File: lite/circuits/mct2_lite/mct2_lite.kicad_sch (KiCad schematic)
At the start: 1 part

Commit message: 20250410-1
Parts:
- added BT?: Battery_Cell, symbol Device:Battery_Cell
- added J?: External BIOS, symbol Connector_Generic:Conn_02x04_Counter_Clockwise
- added J?: TPM, symbol Connector_Generic:Conn_02x05_Odd_Even
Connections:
- net GND: now also BT?.2 (-), J?.4 (Pin_4)
- net SOM_PWRBTN: now reaches A?.1 (~{PWRBTN})
- net SOM_SIO_UART_TX: now reaches A?.10 (SIO_UART_TX)
- net SOM_SMB_ALT: now reaches A?.104 (~{SMB_ALERT})
- net SOM_SMB_SCL: now reaches A?.106 (SMB_CLK)
- net SOM_SMB_SDA: now reaches A?.108 (SMB_DATA)
- net SOM_RTC_BAT: now reaches A?.115 (VBAT)
- net SOM_RTC_BAT: now also BT?.1 (+)
- net SOM_SIO_UART_RX: now reaches A?.12 (SIO_UART_RX)
- net SOM_UART0_RX: now reaches A?.137 (UART0_RXD)
- net SOM_UART2_TX: now reaches A?.138 (UART2_TXD)
- net SOM_UART0_TX: now reaches A?.139 (UART0_TXD)
- net SOM_UART2_RX: now reaches A?.140 (UART2_RXD)
- net SOM_UART1_RX: now reaches A?.141 (UART1_RXD)
- net SOM_UART1_TX: now reaches A?.143 (UART1_TXD)
- net SOM_SML_SDA: now reaches A?.145 (SML1_DATA)
- net SOM_SML_SCL: now reaches A?.147 (SML1_CLK)
- net SOM_SML_ALT: now reaches A?.149 (~{SML1_ALERT})
- net SOM_I2C2_SCL: now reaches A?.154 (I2C2_SCL)
- net SOM_I2C2_SDA: now reaches A?.156 (I2C2_SDA)
- net HDMI_SDA: now reaches A?.169 (DDIB_DDC_SDA)
- net HDMI_SCL: now reaches A?.171 (DDIB_DDC_SCL)
- net HDMI_HPD: now reaches A?.183 (DDIB_HPD)
- net HDMI_AUX_N: now reaches A?.191 (DDIB_AUX-)
- net HDMI_AUX_P: now reaches A?.193 (DDIB_AUX+)
- net HDMI_CLK_N: now reaches A?.197 (DDIB_TX3-)
- net HDMI_CLK_P: now reaches A?.199 (DDIB_TX3+)
- net SOM_FAN1_PWM: now reaches A?.2 (FAN1_PWM)
- net HDMI_TX2_N: now reaches A?.203 (DDIB_TX2-)
- net HDMI_TX2_P: now reaches A?.205 (DDIB_TX2+)
- net HDMI_TX1_N: now reaches A?.209 (DDIB_TX1-)
- net HDMI_TX1_P: now reaches A?.211 (DDIB_TX1+)
- net HDMI_TX0_N: now reaches A?.215 (DDIB_TX0-)
- net HDMI_TX0_P: now reaches A?.217 (DDIB_TX0+)
- net TCP1_TX0_P: now reaches A?.220 (TCP1_TX0+)
- net TCP0_AUX_N: now reaches A?.221 (TCP0_AUX-)
- net TCP1_TX0_N: now reaches A?.222 (TCP1_TX0-)
- net TCP0_AUX_P: now reaches A?.223 (TCP0_AUX+)
- net TCP1_TXRX0_P: now reaches A?.226 (TCP1_TXRX0+)
- net TCP0_TXRX1_N: now reaches A?.227 (TCP0_TXRX1-)
- net TCP1_TXRX0_N: now reaches A?.228 (TCP1_TXRX0-)
- net TCP0_TXRX1_P: now reaches A?.229 (TCP0_TXRX1+)
- net TCP1_TX1_P: now reaches A?.232 (TCP1_TX1+)
- net TCP0_TX1_N: now reaches A?.233 (TCP0_TX1-)
- net TCP1_TX1_N: now reaches A?.234 (TCP1_TX1-)
- net TCP0_TX1_P: now reaches A?.235 (TCP0_TX1+)
- net TCP1_TXRX1_P: now reaches A?.238 (TCP1_TXRX1+)
- net TCP0_TXRX0_N: now reaches A?.239 (TCP0_TXRX0-)
- net TCP1_TXRX1_N: now reaches A?.240 (TCP1_TXRX1-)
- net TCP0_TXRX0_P: now reaches A?.241 (TCP0_TXRX0+)
- net TCP1_AUX_P: now reaches A?.244 (TCP1_AUX+)
- net TCP0_TX0_N: now reaches A?.245 (TCP0_TX0-)
- net TCP1_AUX_N: now reaches A?.246 (TCP1_AUX-)
- net TCP0_TX0_P: now reaches A?.247 (TCP0_TX0+)
- net SOM_RSTBTN: now reaches A?.3 (~{RSTBTN})
- net SOM_FAN1_TAC: now reaches A?.4 (FAN1_TAC)
- net SOM_SIO_SLS_S0: now reaches A?.5 (SLS_S0)
- net SOM_FAN2_PWM: now reaches A?.6 (FAN2_PWM)
- net SOM_SIO_SLS_S3: now reaches A?.7 (SLS_S3)
- net SOM_FAN2_TAC: now reaches A?.8 (FAN2_TAC)
- net SOM_PCIE_REF0_P: now reaches A?.85 (REFCLK0+)
- net SOM_PCIE_REF0_N: now reaches A?.87 (REFCLK0-)
- net SOM_PCIE_REF3_P: now reaches A?.88 (REFCLK3+)
- net SOM_TSENSE: now reaches A?.9 (TSENSE)
- net SOM_PCIE_REF3_N: now reaches A?.90 (REFCLK3-)
- net SOM_PCIE_REF1_P: now reaches A?.91 (REFCLK1+)
- net SOM_PCIE_REF1_N: now reaches A?.93 (REFCLK1-)
- net SOM_PCIE_REF4_P: now reaches A?.94 (REFCLK4+)
- net SOM_PCIE_REF4_N: now reaches A?.96 (REFCLK4-)
- net SOM_PCIE_REF2_P: now reaches A?.97 (REFCLK2+)
- net SOM_PCIE_REF2_N: now reaches A?.99 (REFCLK2-)
- new net SOM_SPI_CLK: J?.6 (Pin_6)
- new net SOM_SPI_CS: J?.1 (Pin_1)
- new net SOM_SPI_IO0_MOSI: J?.5 (Pin_5)
- new net SOM_SPI_IO1_MISO: J?.2 (Pin_2)
- new net SOM_SPI_IO2: J?.3 (Pin_3)
- new net SOM_SPI_IO3: J?.7 (Pin_7)
- new net SOM_SPI_VCC: J?.1 (Pin_1), J?.8 (Pin_8)
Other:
- note added: "2025-03-23 - 2025-03-29"
- note added: "MediaCow Touch 2 Lite - Root"
- note removed: "2025-03-23 - 2025-03-23"
- note removed: "MediaCow Touch 2 - Root"

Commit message: 20250410-2
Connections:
- net SOM_USB2_P1_P: now also A?.69 (USB2_P1+)
- net SOM_USB_OC: now also A?.129 (~{USB_OC})
- net SOM_USB2_P5_N: now reaches A?.109 (USB2_P5-)
- net SOM_USB2_P5_P: now reaches A?.111 (USB2_P5+)
- net SOM_USB2_P6_P: now reaches A?.112 (USB2_P6+)
- net SOM_USB2_P6_N: now reaches A?.114 (USB2_P6-)
- net SOM_PROCHOT: now reaches A?.117 (~{PROCHOT})
- net SOM_SPI_TPM_IRQ: now reaches A?.127 (TPM_IRQ)
- net SOM_SUSCLK: now reaches A?.131 (SUSCLK)
- net SOM_USB2_P1_N: now reaches A?.67 (USB2_P1-)
- net SOM_USB2_P4_P: now reaches A?.70 (USB2_P4+)
- net SOM_USB2_P4_N: now reaches A?.72 (USB2_P4-)
- net SOM_USB2_P2_N: now reaches A?.73 (USB2_P2-)
- net SOM_USB2_P2_P: now reaches A?.75 (USB2_P2+)
- net SOM_USB2_P7_P: now reaches A?.76 (USB2_P7+)
- net SOM_USB2_P7_N: now reaches A?.78 (USB2_P7-)
- net SOM_USB2_P3_N: now reaches A?.79 (USB2_P3-)
- net SOM_USB2_P3_P: now reaches A?.81 (USB2_P3+)
- net SOM_USB2_P8_P: now reaches A?.82 (USB2_P8+)
- net SOM_USB2_P8_N: now reaches A?.84 (USB2_P8-)
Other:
- note added: "2025-03-23 - 2025-04-10"
- note added: "MediaCow Touch 2 Lite "Curitiba" - CTCL 2021-2025"
- note removed: "2025-03-23 - 2025-03-29"
- note removed: "CTCL 2021-2025"

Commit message: 20250410-3
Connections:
- net SOM_SPI_CS: now also A?.165 (~{SPI_CS})
- net SOM_VSYS: now also A?.250 (VIN), A?.251 (VIN), A?.252 (VIN), A?.253 (VIN), A?.254 (VIN), A?.255 (VIN), A?.256 (VIN), A?.257 (VIN), A?.258 (VIN), A?.259 (VIN), A?.260 (VIN)
- net SOM_PCIE_WAKE: now reaches A?.103 (~{WAKE})
- net SOM_PCIE_PLTRST: now reaches A?.105 (~{PLTRST})
- net SOM_SPI_CS2: now reaches A?.157 (~{SPI_CS2})
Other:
- moved on the sheet: J?

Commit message: 20250414-1
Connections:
- net GND: now also J?.6 (Pin_6)
- net SOM_SPI_CLK: now also A?.155 (SPI_CLK), J?.5 (Pin_5)
- net SOM_SPI_CS2: now also J?.2 (Pin_2)
- net SOM_SPI_IO0_MOSI: now also A?.159 (SPI_MOSI/SPI_IO0), J?.7 (Pin_7)
- net SOM_SPI_IO1_MISO: now also A?.163 (SPI_MISO/SPI_IO1), J?.4 (Pin_4)
- net SOM_SPI_IO2: now also A?.161 (SPI_IO2)
- net SOM_SPI_IO3: now also A?.153 (SPI_IO3)
- net SOM_SPI_TPM_IRQ: now also J?.10 (Pin_10)
- net SOM_PCIE_CLKREQ3: now reaches A?.100 (~{CLKREQ3})
- net SOM_PCIE_CLKREQ4: now reaches A?.102 (~{CLKREQ4})
- net SOM_GSX_CLK: now reaches A?.118 (GPP_F16)
- net SOM_SATAXPCIE0: now reaches A?.119 (GPP_E0)
- net SOM_GSX_RESET: now reaches A?.120 (GPP_F15)
- net SOM_SATAXPCIE1: now reaches A?.121 (GPP_A12)
- net SOM_GSX_DIN: now reaches A?.122 (GPP_F14)
- net SOM_SPKR_SATALED: now reaches A?.123 (GPP_B14)
- net SOM_GSX_SLOAD: now reaches A?.124 (GPP_F13)
- net SOM_SML_PMCALT: now reaches A?.125 (GPP_B11)
- net SOM_GSX_DOUT: now reaches A?.126 (GPP_F12)
- net SOM_SBK0: now reaches A?.128 (GPP_D0)
- net SOM_HSIO0_TX_P: now reaches A?.13 (HSIO0_TX+)
- net SOM_SBK1: now reaches A?.130 (GPP_D1)
- net SOM_SBK2: now reaches A?.132 (GPP_D2)
- net SOM_SBK3: now reaches A?.134 (GPP_D3)
- net SOM_HSIO0_TX_N: now reaches A?.15 (HSIO0_TX-)
- net SOM_HSIO0_RX_P: now reaches A?.16 (HSIO0_RX+)
- net SOM_I2S_MCLK: now reaches A?.160 (I2S_MCLK)
- net SOM_I2S_SCLK: now reaches A?.162 (I2S_SCLK)
- net SOM_I2S_SFRM: now reaches A?.164 (I2S_SFRM)
- net SOM_I2S_TXD: now reaches A?.166 (I2S_TXD)
- net SOM_I2S_RXD: now reaches A?.168 (I2S_RXD)
- net SOM_HSIO0_RX_N: now reaches A?.18 (HSIO0_RX-)
- net SOM_HSIO1_TX_P: now reaches A?.19 (HSIO1_TX+)
- net SOM_HSIO1_TX_N: now reaches A?.21 (HSIO1_TX-)
- net SOM_HSIO1_RX_P: now reaches A?.22 (HSIO1_RX+)
- net SOM_HSIO1_RX_N: now reaches A?.24 (HSIO1_RX-)
- net SOM_HSIO2_TX_P: now reaches A?.25 (HSIO2_TX+)
- net SOM_HSIO2_TX_N: now reaches A?.27 (HSIO2_TX-)
- net SOM_HSIO2_RX_P: now reaches A?.28 (HSIO2_RX+)
- net SOM_HSIO2_RX_N: now reaches A?.30 (HSIO2_RX-)
- net SOM_HSIO3_TX_P: now reaches A?.31 (HSIO3_TX+)
- net SOM_HSIO3_TX_N: now reaches A?.33 (HSIO3_TX-)
- net SOM_HSIO3_RX_P: now reaches A?.34 (HSIO3_RX+)
- net SOM_HSIO3_RX_N: now reaches A?.36 (HSIO3_RX-)
- net SOM_HSIO8_TX_P: now reaches A?.37 (HSIO8_TX+)
- net SOM_HSIO8_TX_N: now reaches A?.39 (HSIO8_TX-)
- net SOM_HSIO8_RX_P: now reaches A?.40 (HSIO8_RX+)
- net SOM_HSIO8_RX_N: now reaches A?.42 (HSIO8_RX-)
- net SOM_HSIO9_TX_P: now reaches A?.43 (HSIO9_TX+)
- net SOM_HSIO9_TX_N: now reaches A?.45 (HSIO9_TX-)
- net SOM_HSIO9_RX_P: now reaches A?.46 (HSIO9_RX+)
- net SOM_HSIO9_RX_N: now reaches A?.48 (HSIO9_RX-)
- net SOM_HSIO10_TX_P: now reaches A?.49 (HSIO10_TX+)
- net SOM_HSIO10_TX_N: now reaches A?.51 (HSIO10_TX-)
- net SOM_HSIO10_RX_P: now reaches A?.52 (HSIO10_RX+)
- net SOM_HSIO10_RX_N: now reaches A?.54 (HSIO10_RX-)
- net SOM_HSIO11_TX_P: now reaches A?.55 (HSIO11_TX+)
- net SOM_HSIO11_TX_N: now reaches A?.57 (HSIO11_TX-)
- net SOM_HSIO11_RX_P: now reaches A?.58 (HSIO11_RX+)
- net SOM_HSIO11_RX_N: now reaches A?.60 (HSIO11_RX-)
- net SOM_HSIO6_TX_P: now reaches A?.61 (HSIO6_TX+)
- net SOM_HSIO6_TX_N: now reaches A?.63 (HSIO6_TX-)
- net SOM_HSIO6_RX_P: now reaches A?.64 (HSIO6_RX+)
- net SOM_HSIO6_RX_N: now reaches A?.66 (HSIO6_RX-)
- no-connect marks 0 -> 7
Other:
- note added: "2025-03-23 - 2025-04-14"
- note removed: "2025-03-23 - 2025-04-10"

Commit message: 20250415-1
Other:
- added sheet SMEC (mct2_lite_smec.kicad_sch)
- note added: "2025-03-23 - 2025-04-15"
- note removed: "2025-03-23 - 2025-04-14"
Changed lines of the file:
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@@
 		)
 	)
-	(text "2025-03-23 - 2025-04-14"
+	(text "2025-03-23 - 2025-04-15"
 		(exclude_from_sim no)
 		(at 517.906 403.352 0)
@@
 	)
 	(sheet
+		(at 527.05 361.95)
+		(size 12.7 12.7)
+		(fields_autoplaced yes)
+		(stroke
+			(width 0.1524)
+			(type solid)
+		)
+		(fill
+			(color 0 0 0 0.0000)
+		)
+		(property "Sheetname" "SMEC"
+			(at 527.05 361.2384 0)
+			(effects
+				(font
+					(size 1.27 1.27)
+				)
+				(justify left bottom)
+			)
+		)
+		(property "Sheetfile" "mct2_lite_smec.kicad_sch"
+			(at 527.05 375.2346 0)
+			(effects
+				(font
+					(size 1.27 1.27)
+				)
+				(justify left top)
+			)
+		)
+		(instances
+			(project "mct2_lite"
+				(path "/caf0e9b0-a44c-4a4e-b706-dd9d72690bf9"
+					(page "4")
+				)
+			)
+		)
+	)
+	(sheet
 		(at 546.1 361.95)
 		(size 12.7 12.7)
@@
 	)
 	(sheet
-		(at 564.515 361.95)
-		(size 13.335 12.7)
+		(at 565.15 361.95)
+		(size 12.7 12.7)
 		(fields_autoplaced yes)
 		(stroke
@@
 		)
 		(property "Sheetname" "Power"
-			(at 564.515 361.2384 0)
+			(at 565.15 361.2384 0)
 			(effects
 				(font
@@
 		)
 		(property "Sheetfile" "mct2_lite_power.kicad_sch"
-			(at 564.515 375.2346 0)
+			(at 565.15 375.2346 0)
 			(effects
 				(font

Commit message: 20250423-1
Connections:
- net SOM_SPI_BIOS_SEL: now reaches A?.133 (~{BIOS_SEL})
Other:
- note added: "2025-03-23 - 2025-04-23"
- note removed: "2025-03-23 - 2025-04-15"
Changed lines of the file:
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@@
 	(wire
 		(pts
+			(xy 217.17 242.57) (xy 214.63 242.57)
+		)
+		(stroke
+			(width 0)
+			(type default)
+		)
+	)
+	(wire
+		(pts
 			(xy 130.81 156.21) (xy 133.35 156.21)
 		)
@@
 		)
 	)
-	(text "2025-03-23 - 2025-04-15"
+	(text "2025-03-23 - 2025-04-23"
 		(exclude_from_sim no)
 		(at 517.906 403.352 0)
@@
 				(hide yes)
 			)
+		)
+	)
+	(global_label "SOM_SPI_BIOS_SEL"
+		(shape input)
+		(at 217.17 242.57 0)
+		(fields_autoplaced yes)
+		(effects
+			(font
+				(size 1.27 1.27)
+			)
+			(justify left)
+		)
+		(property "Intersheetrefs" "${INTERSHEET_REFS}"
+			(at 237.9351 242.57 0)
+			(effects
+				(font
+					(size 1.27 1.27)
+				)
+				(justify left)
+				(hide yes)
+			)

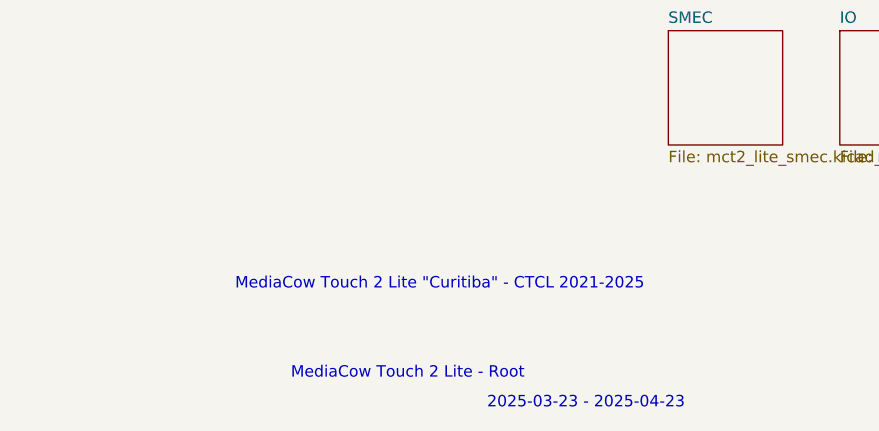
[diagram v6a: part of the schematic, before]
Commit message: 20250426-1 Remove current codename
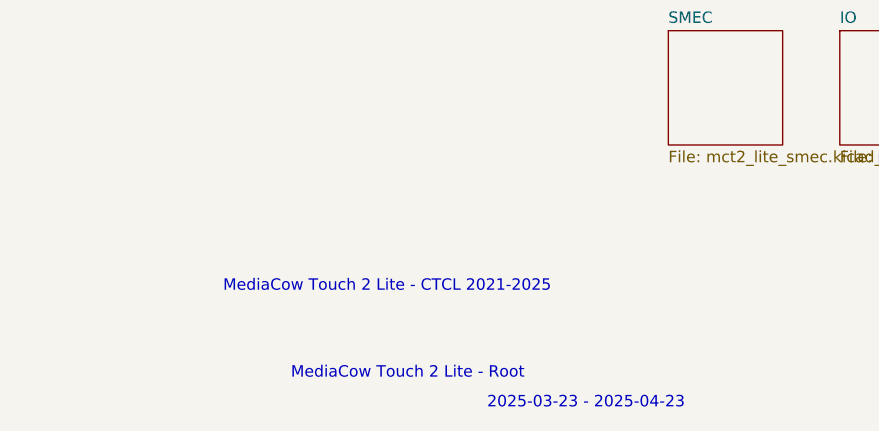
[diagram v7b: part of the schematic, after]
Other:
- note added: "MediaCow Touch 2 Lite - CTCL 2021-2025"
- note removed: "MediaCow Touch 2 Lite "Curitiba" - CTCL 2021-2025"
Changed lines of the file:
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@@
 		)
 	)
-	(text "MediaCow Touch 2 Lite \"Curitiba\" - CTCL 2021-2025"
+	(text "MediaCow Touch 2 Lite - CTCL 2021-2025"
 		(exclude_from_sim no)
-		(at 501.65 390.144 0)
+		(at 495.808 390.398 0)
 		(effects
 			(font

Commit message: 20250504-1
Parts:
- added TP? (x6): TestPoint_Alt, symbol Connector:TestPoint_Alt
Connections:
- net SOM_PWRBTN: now also TP?.1
- net SOM_RSTBTN: now also TP?.1
- net SOM_SIO_SLS_S0: now also TP?.1
- net SOM_SIO_SLS_S3: now also TP?.1
- net SOM_SIO_UART_RX: now also TP?.1
- net SOM_SIO_UART_TX: now also TP?.1
- net SOM_HDA_RST: now reaches A?.172 (HDA_RST)
- net SOM_HDA_BCLK: now reaches A?.174 (HDA_BCLK)
- net SOM_HDA_SYNC: now reaches A?.176 (HDA_SYNC)
- net SOM_HDA_SDOUT: now reaches A?.178 (HDA_SDOUT)
- net SOM_HDA_SDIN: now reaches A?.180 (HDA_SDIN)
- net SOM_CSI_D_CLK_P: now reaches A?.184 (CSI_D_CK+)
- net SOM_CSI_D_CLK_N: now reaches A?.186 (CSI_D_CK-)
- net SOM_CSI_D_D1_P/C_D2_P: now reaches A?.190 (CSI_D_D1+/CSI_C_D2+)
- net SOM_CSI_D_D1_N/C_D2_N: now reaches A?.192 (CSI_D_D1-/CSI_C_D2-)
- net SOM_CSI_D_D0_P/C_D3_P: now reaches A?.196 (CSI_D_D0+/CSI_C_D3+)
- net SOM_CSI_D_D0_N/C_D3_N: now reaches A?.198 (CSI_D_D0-/CSI_C_D3-)
- net SOM_CSI_C_CLK_P: now reaches A?.202 (CSI_C_CK+)
- net SOM_CSI_C_CLK_N: now reaches A?.204 (CSI_C_CK-)
- net SOM_CSI_C_D1_P: now reaches A?.208 (CSI_C_D1+)
- net SOM_CSI_C_D1_N: now reaches A?.210 (CSI_C_D1-)
- net SOM_CSI_C_D0_P: now reaches A?.214 (CSI_C_D0+)
- net SOM_CSI_C_D0_N: now reaches A?.216 (CSI_C_D0-)
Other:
- note added: "2025-03-23 - 2025-04-29"
- note added: "MediaCow Touch 2 Lite "Curitiba" - CTCL 2021-2025"
- note removed: "2025-03-23 - 2025-04-23"
- note removed: "MediaCow Touch 2 Lite - CTCL 2021-2025"
